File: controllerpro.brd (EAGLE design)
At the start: 92.7 x 33.7 mm, 10 parts

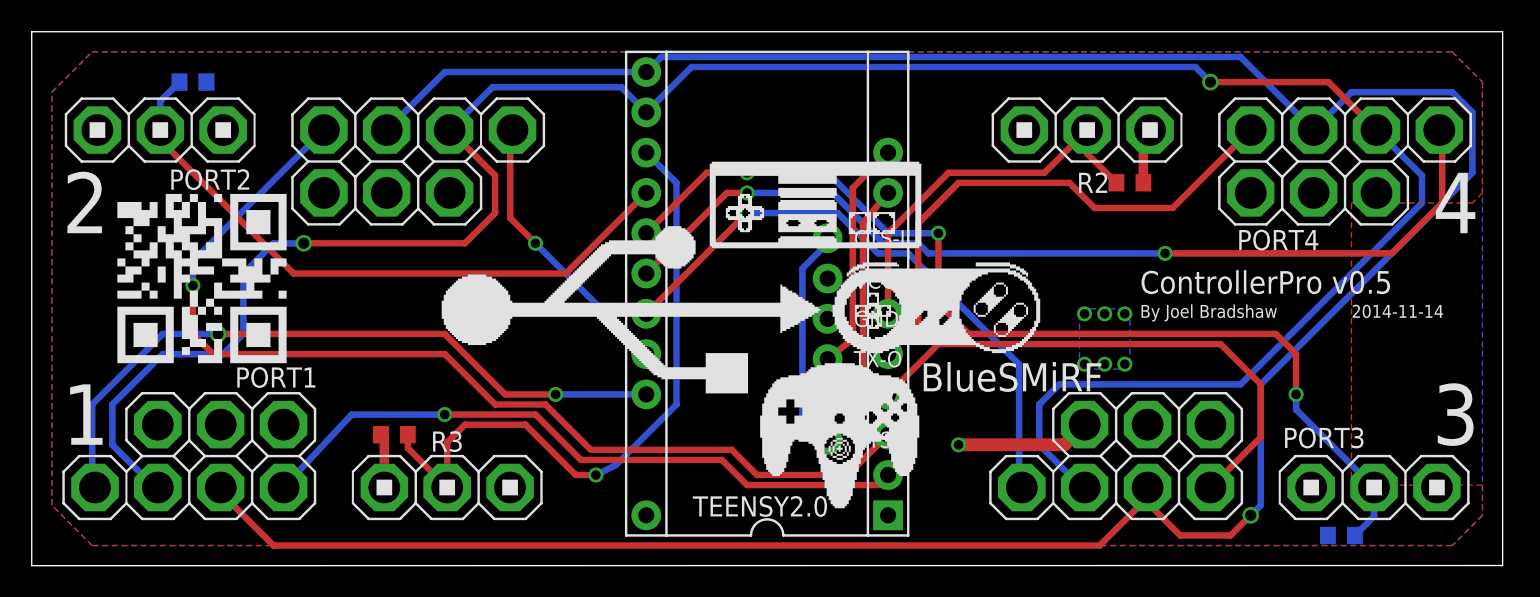
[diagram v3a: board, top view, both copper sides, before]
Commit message: Do some basic simplifications afforded by 3.3V switch
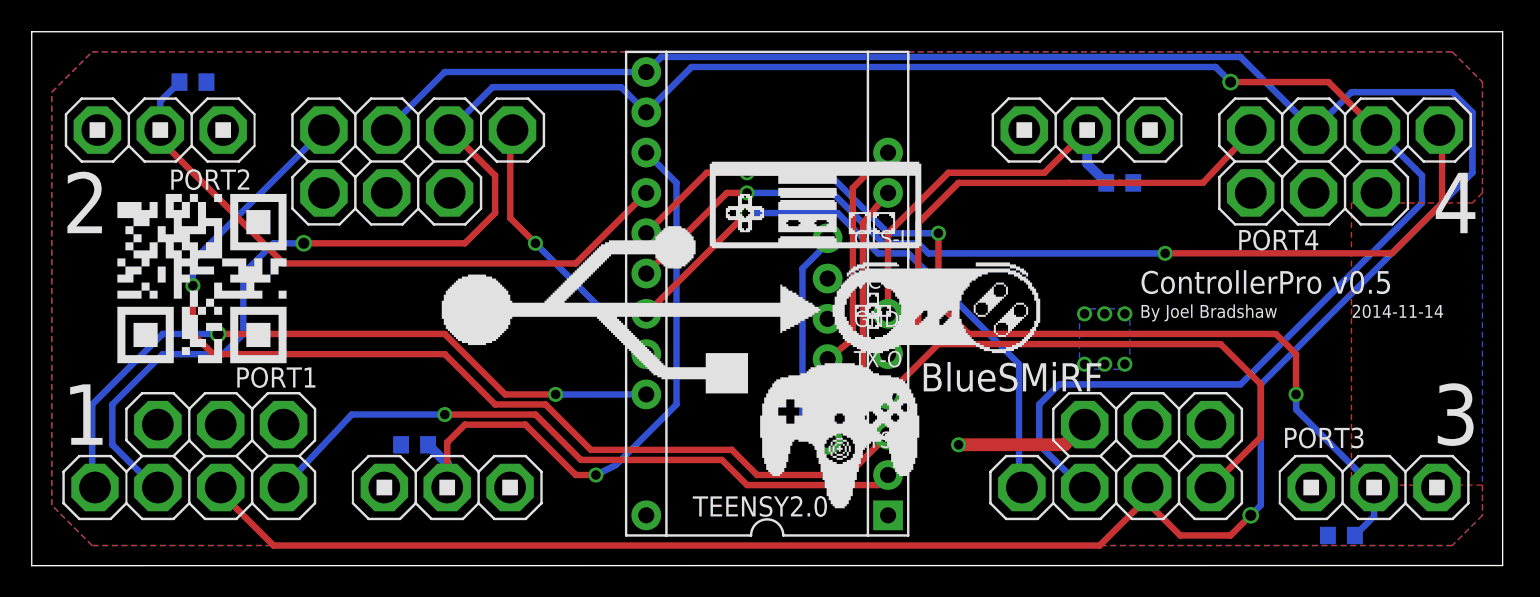
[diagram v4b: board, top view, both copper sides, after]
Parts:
- moved R3 1.42 mm to (24.1, 7.62), flipped to the bottom, turned to 0 degrees
- moved R2 0.64 mm to (68.6, 24.1), flipped to the bottom, turned to 0 degrees
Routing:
- net VCC: track 15.4 -> 8.48 mm
- net 5VDATA1: track 33.7 -> 32.6 mm
- net 3VDATA2: track 41.8 -> 40.7 mm
- net 3VDATA3: track 40.4 -> 39.9 mm
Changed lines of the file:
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@@
 <attribute name="VALUE" x="10.795" y="28.575" size="1.27" layer="28" rot="MR0"/>
 </element>
-<element name="R2" library="rcl" package="R0603" value="10k" x="69.215" y="24.13" smashed="yes" rot="R180">
-<attribute name="NAME" x="67.945" y="24.765" size="1.27" layer="25" rot="R180"/>
-<attribute name="VALUE" x="71.12" y="22.86" size="1.27" layer="27" rot="R180"/>
+<element name="R2" library="rcl" package="R0603" value="10k" x="68.58" y="24.13" smashed="yes" rot="MR0">
+<attribute name="NAME" x="67.31" y="23.495" size="1.27" layer="26" rot="MR0"/>
+<attribute name="VALUE" x="70.485" y="25.4" size="1.27" layer="28" rot="MR0"/>
 </element>
 <element name="R1" library="rcl" package="R0603" value="10k" x="82.55" y="1.905" smashed="yes" rot="MR0">
@@
 <attribute name="VALUE" x="83.185" y="0" size="1.27" layer="28" rot="MR0"/>
 </element>
-<element name="R3" library="rcl" package="R0603" value="10k" x="22.86" y="8.255" smashed="yes" rot="R180">
-<attribute name="NAME" x="27.2288" y="8.4582" size="1.27" layer="25" rot="R180"/>
-<attribute name="VALUE" x="23.495" y="10.16" size="1.27" layer="27" rot="R180"/>
+<element name="R3" library="rcl" package="R0603" value="10k" x="24.13" y="7.62" smashed="yes" rot="MR0">
+<attribute name="NAME" x="28.4988" y="7.4168" size="1.27" layer="26" rot="MR0"/>
+<attribute name="VALUE" x="24.765" y="5.715" size="1.27" layer="28" rot="MR0"/>
 </element>
 <element name="U$1" library="SparkFun-Boards" package="RN42" value="RN42" x="50.165" y="14.2875" rot="MR0"/>
@@
 <wire x1="81.7372" y1="30.48" x2="84.7598" y2="27.4574" width="0.4064" layer="1"/>
 <wire x1="29.0449" y1="30.1625" x2="26.3398" y2="27.4574" width="0.4064" layer="16"/>
-<wire x1="41.5925" y1="31.4325" x2="73.3425" y2="31.4325" width="0.4064" layer="16"/>
-<wire x1="73.3425" y1="31.4325" x2="74.295" y2="30.48" width="0.4064" layer="16"/>
-<via x="74.295" y="30.48" extent="1-16" drill="0.7"/>
-<wire x1="74.295" y1="30.48" x2="81.7372" y2="30.48" width="0.4064" layer="1"/>
+<wire x1="41.5925" y1="31.4325" x2="74.6125" y2="31.4325" width="0.4064" layer="16"/>
+<wire x1="74.6125" y1="31.4325" x2="75.565" y2="30.48" width="0.4064" layer="16"/>
+<via x="75.565" y="30.48" extent="1-16" drill="0.7"/>
+<wire x1="75.565" y1="30.48" x2="81.7372" y2="30.48" width="0.4064" layer="1"/>
 <wire x1="29.0449" y1="30.1625" x2="37.1475" y2="30.1625" width="0.4064" layer="16"/>
 <wire x1="37.1475" y1="30.1625" x2="38.735" y2="28.575" width="0.4064" layer="16"/>
@@
 <contactref element="R4" pad="1"/>
 <contactref element="PORT2" pad="5"/>
-<wire x1="22.225" y1="4.9276" x2="22.225" y2="8.04" width="0.6096" layer="1"/>
-<wire x1="22.225" y1="8.04" x2="22.01" y2="8.255" width="0.6096" layer="1"/>
-<wire x1="70.065" y1="24.13" x2="70.065" y2="27.0374" width="0.6096" layer="1"/>
-<wire x1="70.065" y1="27.0374" x2="70.485" y2="27.4574" width="0.6096" layer="1"/>
 </signal>
 <signal name="GND" class="1">
@@
 <contactref element="PORT4" pad="4"/>
 <wire x1="55.88" y1="15.24" x2="55.88" y2="21.59" width="0.4064" layer="1"/>
-<wire x1="71.9226" y1="22.545" x2="76.835" y2="27.4574" width="0.4064" layer="1"/>
-<wire x1="71.9226" y1="22.545" x2="66.99" y2="22.545" width="0.4064" layer="1"/>
-<wire x1="66.99" y1="22.545" x2="65.405" y2="24.13" width="0.4064" layer="1"/>
+<wire x1="73.8276" y1="24.1325" x2="76.2" y2="26.67" width="0.4064" layer="1"/>
+<wire x1="76.2" y1="26.67" x2="76.835" y2="27.305" width="0.4064" layer="1"/>
+<wire x1="76.835" y1="27.305" x2="76.835" y2="27.4574" width="0.4064" layer="1"/>
+<wire x1="73.8276" y1="24.1325" x2="68.5775" y2="24.1325" width="0.4064" layer="1"/>
+<wire x1="68.5775" y1="24.1325" x2="65.405" y2="24.13" width="0.4064" layer="1"/>
 <wire x1="65.405" y1="24.13" x2="58.42" y2="24.13" width="0.4064" layer="1"/>
 <wire x1="58.42" y1="24.13" x2="55.88" y2="21.59" width="0.4064" layer="1"/>
@@
 <wire x1="34.6075" y1="6.6675" x2="31.75" y2="9.525" width="0.4064" layer="1"/>
 <wire x1="31.75" y1="9.525" x2="26.035" y2="9.525" width="0.4064" layer="1"/>
+<wire x1="20.1676" y1="9.525" x2="15.875" y2="4.9276" width="0.4064" layer="16"/>
 <wire x1="26.035" y1="9.525" x2="20.1676" y2="9.525" width="0.4064" layer="16"/>
-<wire x1="20.1676" y1="9.525" x2="15.875" y2="4.9276" width="0.4064" layer="16"/>
 <via x="26.035" y="9.525" extent="1-16" drill="0.6"/>
 </signal>
@@
 <contactref element="R2" pad="2"/>
 <contactref element="PORT4" pad="6"/>
-<wire x1="66.5226" y1="27.4574" x2="66.5226" y2="25.9724" width="0.4064" layer="1"/>
-<wire x1="66.5226" y1="25.9724" x2="68.365" y2="24.13" width="0.4064" layer="1"/>
 <wire x1="53.975" y1="15.875" x2="53.975" y2="20.955" width="0.4064" layer="1"/>
 <wire x1="53.975" y1="20.955" x2="57.785" y2="24.765" width="0.4064" layer="1"/>
 <wire x1="57.785" y1="24.765" x2="63.8302" y2="24.765" width="0.4064" layer="1"/>
 <wire x1="63.8302" y1="24.765" x2="66.5226" y2="27.4574" width="0.4064" layer="1"/>
+<wire x1="67.73" y1="24.13" x2="66.5226" y2="25.3374" width="0.6096" layer="16"/>
+<wire x1="66.5226" y1="25.3374" x2="66.5226" y2="27.4574" width="0.6096" layer="16"/>
 </signal>
 <signal name="3VDATA2">
@@
 <contactref element="R3" pad="1"/>
 <contactref element="PORT1" pad="6"/>
-<wire x1="23.71" y1="8.255" x2="23.71" y2="7.405" width="0.4064" layer="1"/>
 <wire x1="26.1874" y1="4.9276" x2="26.1874" y2="7.7724" width="0.4064" layer="1"/>
 <wire x1="26.1874" y1="7.7724" x2="27.305" y2="8.89" width="0.4064" layer="1"/>
@@
 <wire x1="40.64" y1="10.16" x2="40.64" y2="24.13" width="0.4064" layer="16"/>
 <wire x1="40.64" y1="24.13" x2="38.735" y2="26.035" width="0.4064" layer="16"/>
-<wire x1="23.71" y1="7.405" x2="26.1874" y2="4.9276" width="0.4064" layer="1"/>
 <via x="35.56" y="5.715" extent="1-16" drill="0.6"/>
 <wire x1="27.305" y1="8.89" x2="31.115" y2="8.89" width="0.4064" layer="1"/>
 <wire x1="31.115" y1="8.89" x2="34.29" y2="5.715" width="0.4064" layer="1"/>
 <wire x1="34.29" y1="5.715" x2="35.56" y2="5.715" width="0.4064" layer="1"/>
+<wire x1="24.98" y1="7.62" x2="26.1874" y2="6.4126" width="0.6096" layer="16"/>
+<wire x1="26.1874" y1="6.4126" x2="26.1874" y2="4.9276" width="0.6096" layer="16"/>
 </signal>
 <signal name="3VDATA3">
@@
 <contactref element="PORT2" pad="6"/>
 <wire x1="8.255" y1="27.305" x2="8.255" y2="26.67" width="0.4064" layer="1"/>
-<wire x1="8.255" y1="26.67" x2="16.51" y2="18.415" width="0.4064" layer="1"/>
+<wire x1="8.255" y1="26.67" x2="15.875" y2="19.05" width="0.4064" layer="1"/>
 <wire x1="8.1026" y1="27.4574" x2="8.1026" y2="29.2726" width="0.4064" layer="16"/>
-<wire x1="16.51" y1="18.415" x2="33.655" y2="18.415" width="0.4064" layer="1"/>
-<wire x1="33.655" y1="18.415" x2="38.735" y2="23.495" width="0.4064" layer="1"/>
+<wire x1="15.875" y1="19.05" x2="34.29" y2="19.05" width="0.4064" layer="1"/>
+<wire x1="34.29" y1="19.05" x2="38.735" y2="23.495" width="0.4064" layer="1"/>
 <wire x1="8.1026" y1="29.2726" x2="9.31" y2="30.48" width="0.4064" layer="16"/>
 <wire x1="8.255" y1="27.305" x2="8.1026" y2="27.4574" width="0.4064" layer="1"/>
